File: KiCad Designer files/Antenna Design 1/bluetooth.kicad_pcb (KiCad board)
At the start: 32 copper layers, 37.8 x 52.3 mm, 56 parts, among them U1 Multi-protocol Bluetooth Low 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, U1 O, U10 O, U102 O, U11 O, U12 O, U13 O, U14 O, U15 O, U16 O, U17 O, U18 O, U19 O, U2 O, U20 O, U21 O, U23 O, U24 O, U25 O, U26 O, U27 O, U28 O, U29 O, U3 O, U30 O, U31 O, U32 O, U33 O, U4 O, U5 O, U6 O, U7 O, U8 O, U9 O

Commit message: changed details
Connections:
- Cap_1 pad 2: Net-(Cap_1-Pad2) -> GND
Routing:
- net GND: track 12.1 -> 80.2 mm, vias 91 -> 115
- net (no net): track 451.2 -> 394.0 mm, vias 17 -> 7
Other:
- board size 37.8 x 52.3 mm -> 42.7 x 45 mm

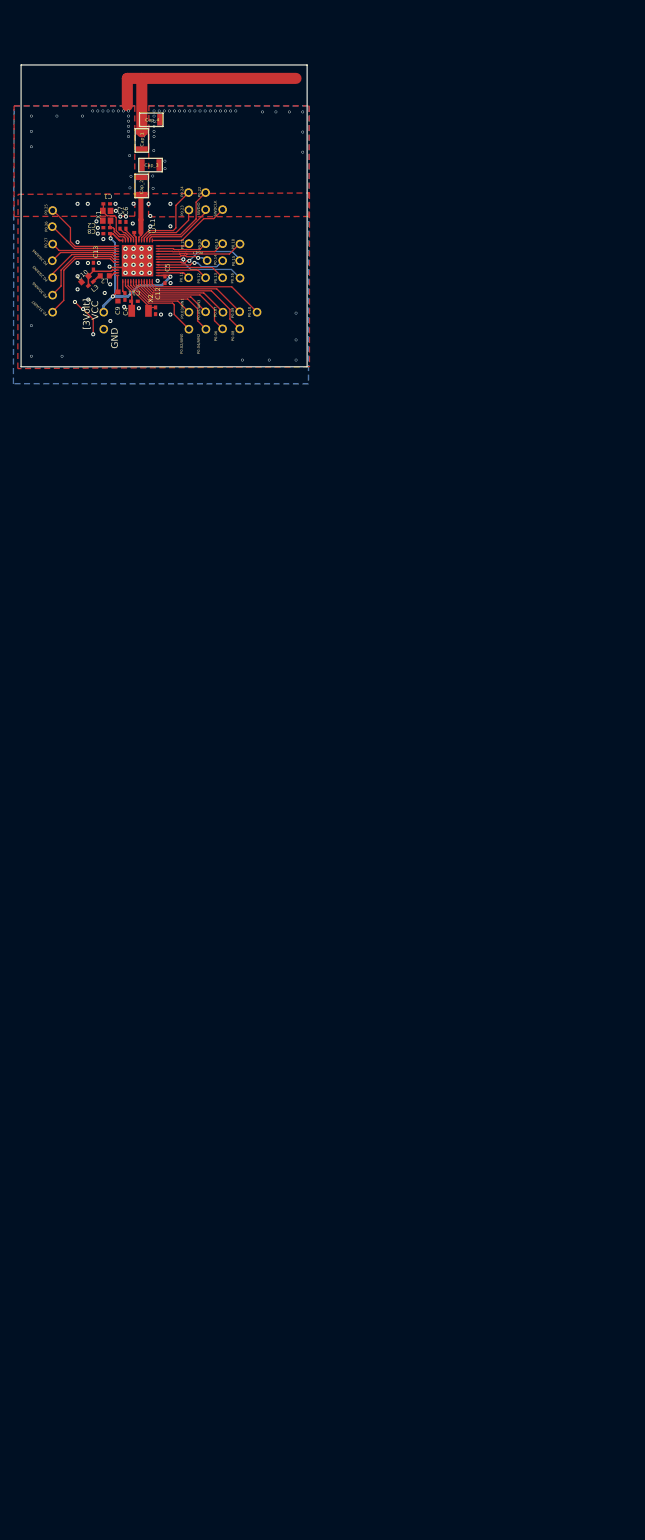
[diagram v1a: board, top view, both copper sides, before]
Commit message: changed pcb position to the center of the pcbnew
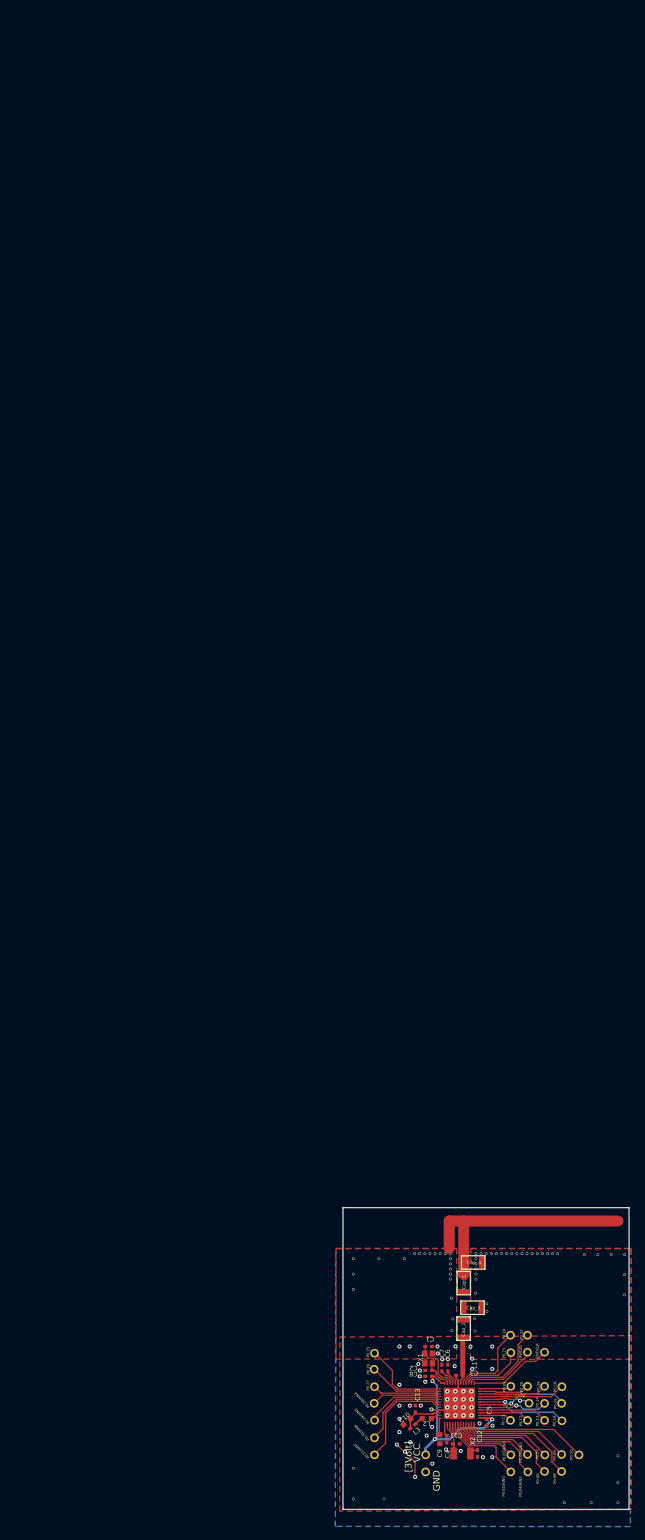
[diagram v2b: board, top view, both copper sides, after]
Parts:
- moved C10 177.0 mm to (131.7, 107.7)
- moved C4 177.0 mm to (137.7, 110.3)
- moved C9 177.0 mm to (136.6, 110.3)
- moved L3 177.0 mm to (132.6, 108.4)
- moved U5 177.0 mm to (126.8, 110.1)
- moved C1 177.0 mm to (134.9, 96.5)
- moved C11 177.0 mm to (139.1, 111.0)
- moved C12 177.0 mm to (142.2, 112.4)
- moved C13 177.0 mm to (133.0, 105.8)
- moved C2 177.0 mm to (134.9, 100.1)
- moved C3 177.0 mm to (139.5, 100.8)
- moved C5 177.0 mm to (143.6, 107.8)
- moved C6 177.0 mm to (137.8, 99.7)
- moved C7 177.0 mm to (136.9, 99.7)
- moved C8 177.0 mm to (134.9, 100.9)
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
